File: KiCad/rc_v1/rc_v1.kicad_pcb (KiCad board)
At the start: 2 copper layers, 122 x 46 mm, 36 parts, among them SW1 SLW-1276864-4A-D, SW10 TS12-66, SW11 TS12-1212, SW12 TS12-1212, SW3 TS12-66, SW4 TS12-66, SW5 TS12-66, SW6 TS12-66, SW7 TS12-66, SW8 TS12-66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

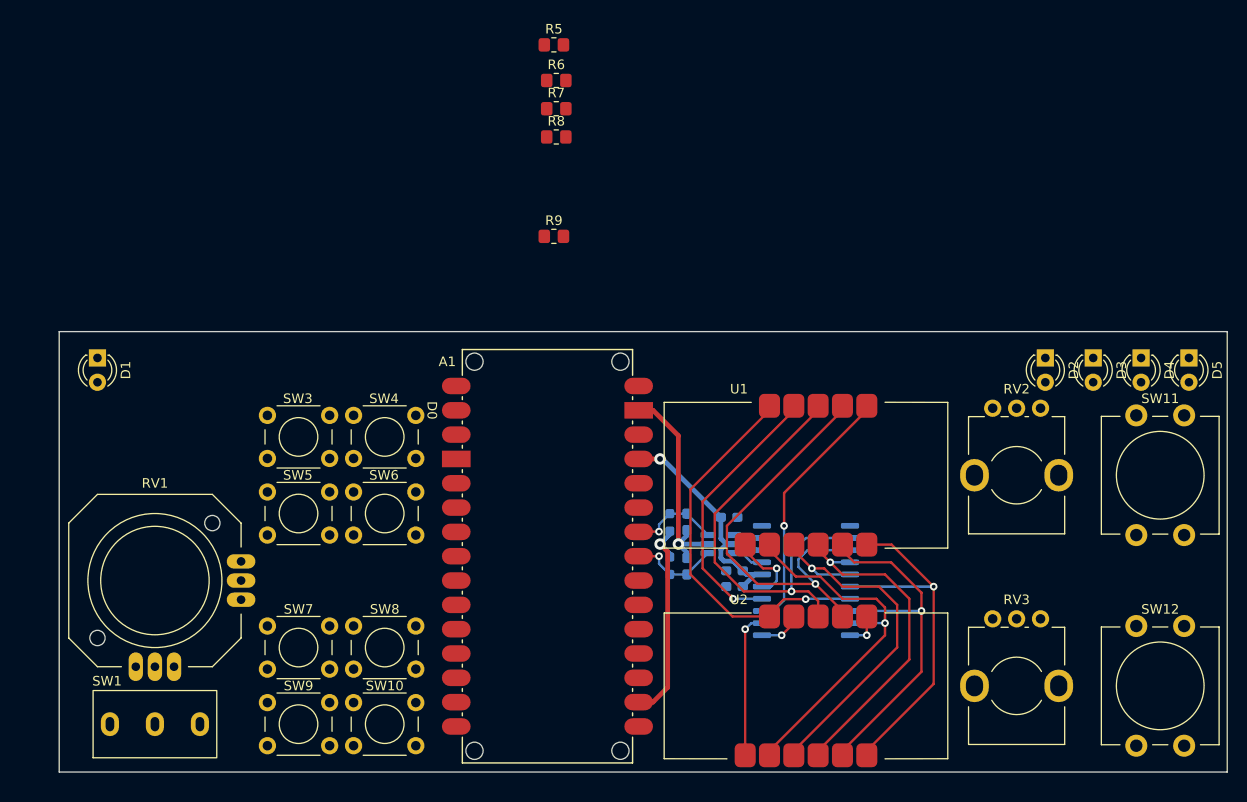
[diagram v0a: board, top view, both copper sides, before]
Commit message: Remote Controller PCB Milestone 2
Routed right side inputs
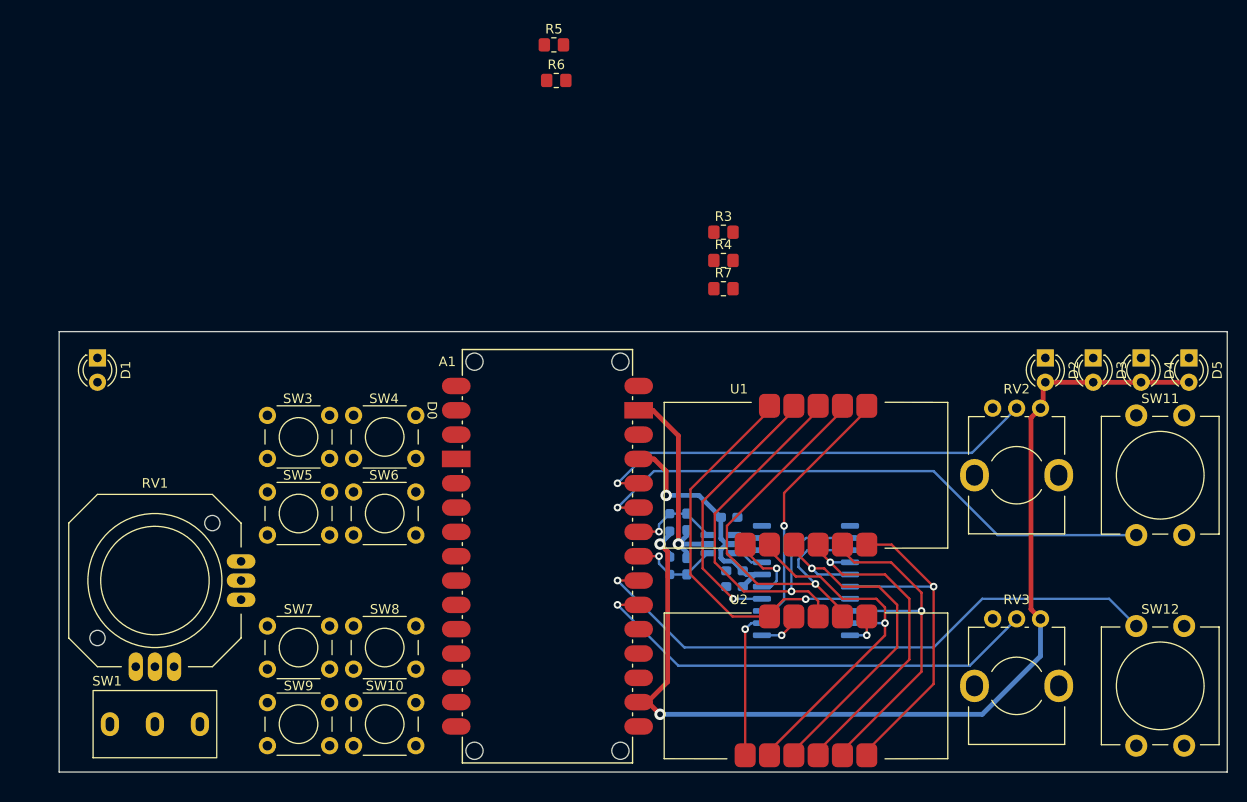
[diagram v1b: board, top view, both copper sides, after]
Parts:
- removed R8, R9: 52.3, Resistor_SMD:R_0805_2012Metric_Pad1.20x1.40mm_HandSolder
- added R3: 52.3, Resistor_SMD:R_0805_2012Metric_Pad1.20x1.40mm_HandSolder, F.Cu at (161.6, 66.5)
- added R4: 52.3, Resistor_SMD:R_0805_2012Metric_Pad1.20x1.40mm_HandSolder, F.Cu at (161.6, 69.4)
- moved R7 25.7 mm to (161.6, 72.4)
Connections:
- A1 pad A0: unconnected-(A1-PadA0) -> /A0
- A1 pad A1: unconnected-(A1-PadA1) -> /A1
- A1 pad A2: unconnected-(A1-PadA2) -> /A2
- A1 pad A3: unconnected-(A1-PadA3) -> /A3
- A1 pad A6: unconnected-(A1-PadA6) -> /A6
- A1 pad A7: unconnected-(A1-PadA7) -> /A7
- D2 pad 1: unconnected-(D2-K-Pad1) -> Net-(D2-K)
- D2 pad 2: unconnected-(D2-A-Pad2) -> +3.3V
- D3 pad 1: unconnected-(D3-K-Pad1) -> Net-(D3-K)
- D3 pad 2: unconnected-(D3-A-Pad2) -> +3.3V
- D4 pad 1: unconnected-(D4-K-Pad1) -> Net-(D4-K)
- D4 pad 2: unconnected-(D4-A-Pad2) -> +3.3V
- D5 pad 1: unconnected-(D5-K-Pad1) -> Net-(D5-K)
- D5 pad 2: unconnected-(D5-A-Pad2) -> +3.3V
- R5 pad 1: unconnected-(R5-Pad1) -> Net-(D3-K)
- R6 pad 1: unconnected-(R6-Pad1) -> Net-(D4-K)
- R7 pad 1: unconnected-(R7-Pad1) -> Net-(D5-K)
- RV2 pad 1: unconnected-(RV2-Pad1) -> +3.3V
- RV2 pad 2: unconnected-(RV2-Pad2) -> /A7
- RV2 pad 3: unconnected-(RV2-Pad3) -> GND
- RV3 pad 1: unconnected-(RV3-Pad1) -> +3.3V
- RV3 pad 2: unconnected-(RV3-Pad2) -> /A2
- RV3 pad 3: unconnected-(RV3-Pad3) -> GND
- SW11 pad 1: unconnected-(SW11-Pad1) -> /A6
- SW11 pad 2: unconnected-(SW11-Pad2) -> GND
- SW12 pad 1: unconnected-(SW12-Pad1) -> /A3
- SW12 pad 2: unconnected-(SW12-Pad2) -> GND
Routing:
- net +3.3V: track 22.5 -> 111.8 mm, vias 1 -> 2
- net /A3: track 0.00 -> 62.6 mm, vias 0 -> 1
- net /A6: track 0.00 -> 60.7 mm, vias 0 -> 1
- net /A2: track 0.00 -> 48.6 mm, vias 0 -> 1
- net /A7: track 0.00 -> 47.1 mm, vias 0 -> 1
- net +5V: track 24.1 -> 25.6 mm

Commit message: Remote Controller PCB Milestone 3
Tentatively completed all connections
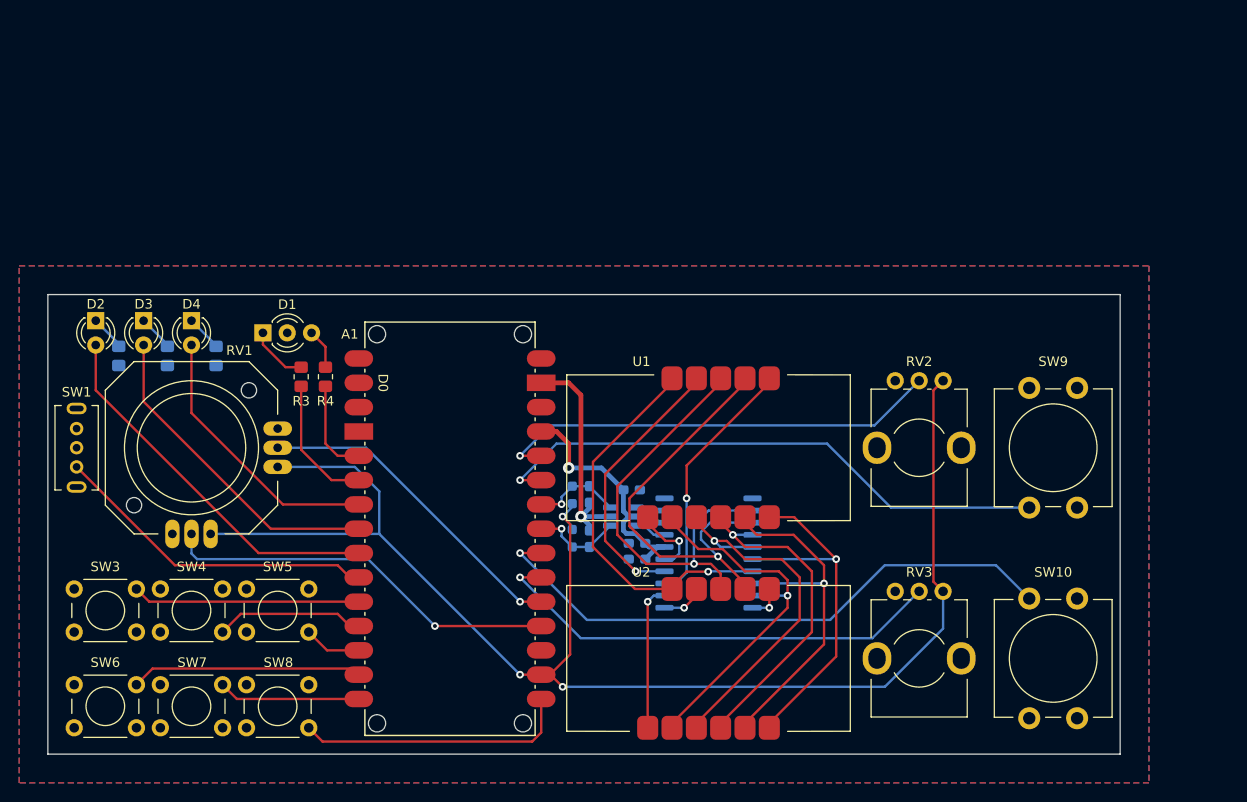
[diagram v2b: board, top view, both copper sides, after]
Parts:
- removed D5: 151031, LED_THT:LED_D3.0mm
- removed the SW10 at (122.9, 115.6)
- removed the SW9 at (113.9, 115.6)
- D1: value 151031 -> LTL1BEKVJNN; footprint LED_THT:LED_D3.0mm -> LED_THT:LED_D3.0mm-3
- R5, R6, R7: moved to B.Cu
- SW1: value SLW-1276864-4A-D -> OS102011MS2Qxxx; footprint Footprint Library:SW_Slide_SPDT_CIT_SLW-1276864-4A-D -> Footprint Library:SW_Slide_SPDT_CK_OS102011MS2Qxxx
- moved D2 99.3 mm to (96.0, 75.7)
- moved D3 99.3 mm to (101.0, 75.7)
- moved D4 99.3 mm to (106.0, 75.7)
- moved R5 55.9 mm to (98.4, 79.4), turned to -90 degrees
- moved R7 53.5 mm to (108.6, 79.4), turned to -90 degrees
- moved R6 49.8 mm to (103.5, 79.4), turned to -90 degrees
- moved R3 46.6 mm to (117.5, 81.6), turned to 90 degrees
- moved R4 43.3 mm to (120.0, 81.6), turned to 90 degrees
- moved SW6 35.4 mm to (93.8, 113.8)
- moved SW1 31.1 mm to (94.0, 87.0), turned to 0 degrees
- moved SW3 27.1 mm to (93.8, 103.8)
- moved SW4 27.1 mm to (102.8, 103.8)
- moved D1 17.5 mm to (113.5, 77.0), turned to 0 degrees
- moved RV1 14.4 mm to (106.0, 89.0)
- moved SW7 12.8 mm to (102.8, 113.8)
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- renumbered SW12 to SW10, SW11 to SW9
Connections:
- A1 pad D10: unconnected-(A1-PadD10) -> /D10
- A1 pad D11: unconnected-(A1-D11_MOSI-PadD11) -> /D11
- A1 pad D12: unconnected-(A1-D12_MISO-PadD12) -> /D12
- A1 pad D13: unconnected-(A1-D13_SCK-PadD13) -> /D13
- A1 pad D2: unconnected-(A1-PadD2) -> /D2
- A1 pad D3: unconnected-(A1-PadD3) -> /D3
- A1 pad D4: unconnected-(A1-PadD4) -> /D4
- A1 pad D5: unconnected-(A1-PadD5) -> /D5
- A1 pad D6: unconnected-(A1-PadD6) -> /D6
- A1 pad D7: unconnected-(A1-PadD7) -> /D7
- A1 pad D8: unconnected-(A1-PadD8) -> /D8
- A1 pad D9: unconnected-(A1-PadD9) -> /D9
- D1 pad 1: unconnected-(D1-K-Pad1) -> Net-(D1-A1)
- D1 pad 2: unconnected-(D1-A-Pad2) -> GND
- D2 pad 2: +3.3V -> /D6
- D3 pad 2: +3.3V -> /D5
- D4 pad 2: +3.3V -> /D4
- R3 pad 1: unconnected-(R3-Pad1) -> /D3
- R3 pad 2: unconnected-(R3-Pad2) -> Net-(D1-A1)
- R4 pad 1: Net-(D2-K) -> /D2
- R4 pad 2: unconnected-(R4-Pad2) -> Net-(D1-A2)
- R5 pad 1: Net-(D3-K) -> Net-(D2-K)
- R5 pad 2: unconnected-(R5-Pad2) -> GND
- R6 pad 1: Net-(D4-K) -> Net-(D3-K)
- R6 pad 2: unconnected-(R6-Pad2) -> GND
- R7 pad 1: Net-(D5-K) -> Net-(D4-K)
- R7 pad 2: unconnected-(R7-Pad2) -> GND
- RV1 pad 1: unconnected-(RV1-Pad1) -> GND
- RV1 pad 2: unconnected-(RV1-Pad2) -> /A1
- RV1 pad 3: unconnected-(RV1-Pad3) -> +3.3V
- RV1 pad 4: unconnected-(RV1-Pad4) -> GND
- RV1 pad 5: unconnected-(RV1-Pad5) -> /A0
- RV1 pad 6: unconnected-(RV1-Pad6) -> +3.3V
- SW1 pad 2: unconnected-(SW1-B-Pad2) -> GND
- SW1 pad 3: unconnected-(SW1-C-Pad3) -> /D7
- SW3 pad 1: unconnected-(SW3-Pad1) -> /D8
- SW3 pad 2: unconnected-(SW3-Pad2) -> GND
- SW4 pad 1: unconnected-(SW4-Pad1) -> GND
- SW4 pad 2: unconnected-(SW4-Pad2) -> /D9
- SW5 pad 1: unconnected-(SW5-Pad1) -> GND
- SW5 pad 2: unconnected-(SW5-Pad2) -> /D10
- SW6 pad 1: unconnected-(SW6-Pad1) -> /D11
- SW6 pad 2: unconnected-(SW6-Pad2) -> GND
- SW7 pad 1: unconnected-(SW7-Pad1) -> /D12
- SW7 pad 2: unconnected-(SW7-Pad2) -> GND
- SW8 pad 1: unconnected-(SW8-Pad1) -> GND
- SW8 pad 2: unconnected-(SW8-Pad2) -> /D13
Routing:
- net /A0: track 0.00 -> 41.7 mm, vias 0 -> 1
- net /D6: track 0.00 -> 39.2 mm
- net +3.3V: track 111.8 -> 150.6 mm, vias 2 -> 3
- net /D7: track 0.00 -> 34.3 mm
- net /A1: track 0.00 -> 34.2 mm, vias 0 -> 1
- net /D5: track 0.00 -> 33.9 mm
- net /D13: track 0.00 -> 28.8 mm
- net /D4: track 0.00 -> 28.5 mm
- net /D11: track 0.00 -> 24.2 mm
- net /D8: track 0.00 -> 23.8 mm
- net /D9: track 0.00 -> 15.5 mm
- net /D12: track 0.00 -> 14.8 mm
- net /D3: track 0.00 -> 14.0 mm
- net /D2: track 0.00 -> 9.99 mm
- net Net-(D1-A1): track 0.00 -> 6.20 mm
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- added copper zone on B.Cu, net GND
- added copper zone on F.Cu, net GND
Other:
- board size 122 x 46 mm -> 112 x 48 mm

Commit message: Backup
Will replace buffer with level shifter
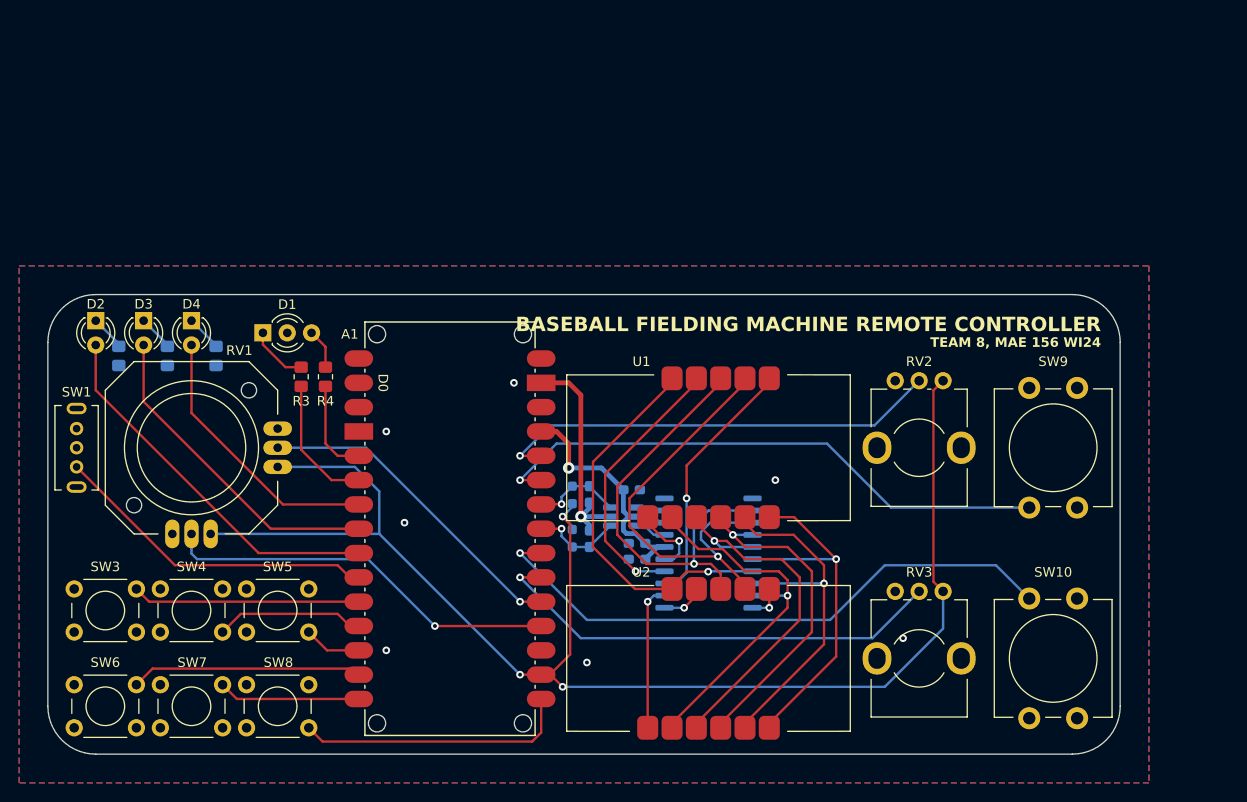
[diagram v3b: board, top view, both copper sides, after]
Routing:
- net GND: vias 1 -> 8
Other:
- outline, holes or cut-outs redrawn
- board text added: "BASEBALL FIELDING MACHINE REMOTE CONTROLLER"
- board text added: "D.H.L. REV. 0 01/04/2024"
- board text added: "TEAM 8, MAE 156 WI24"

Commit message: Remote Controller PCB Milestone 5
Added level shifter IC, prototype board nearly completed
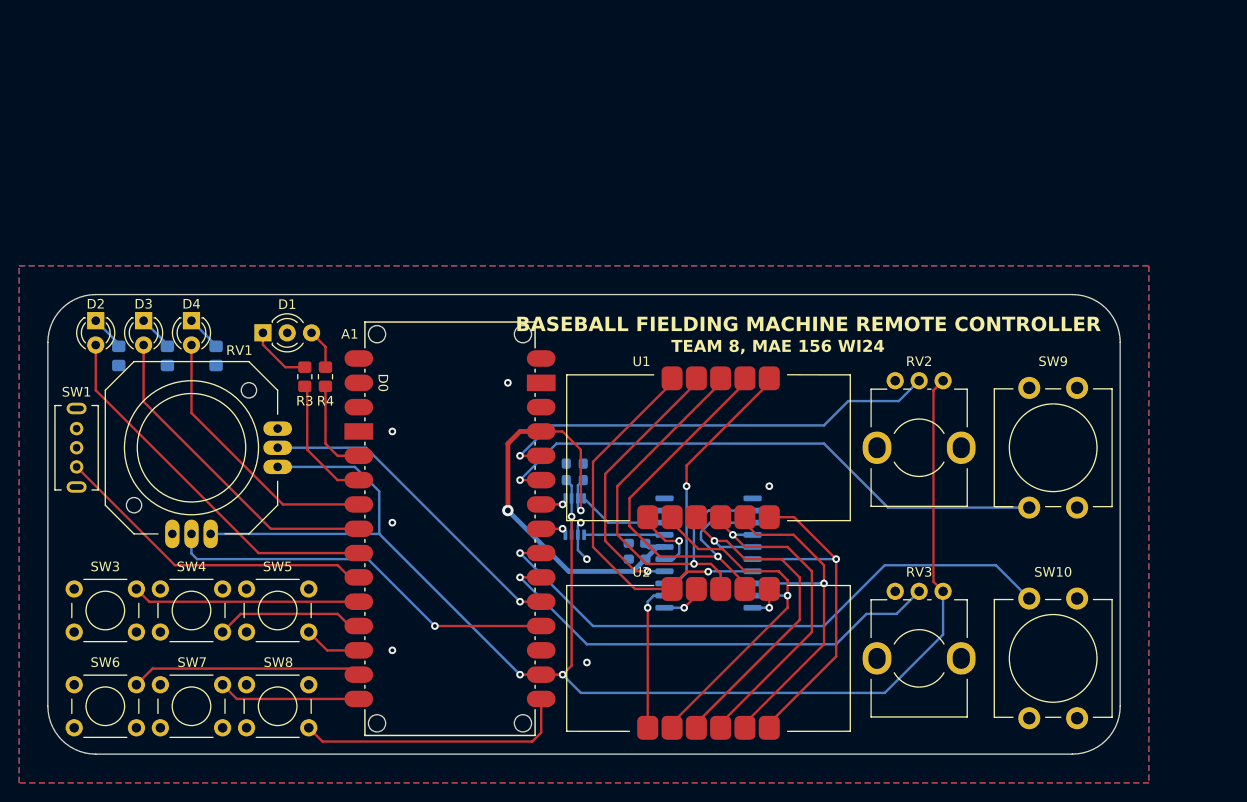
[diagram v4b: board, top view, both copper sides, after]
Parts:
- removed C5: 0.1u, Capacitor_SMD:C_0603_1608Metric_Pad1.08x0.95mm_HandSolder
- removed R1, R2: 10k, Resistor_SMD:R_0603_1608Metric_Pad0.98x0.95mm_HandSolder
- removed U6: SN74LVC2G17DBVR, Footprint Library:SOT-23-6_HandSoldering_Rounded
- added U4: TXS0102DCTR, Footprint Library:SSOP-8_2.95x2.8mm_P0.65mm, B.Cu at (146.0, 96.2)
- C3, C4: value 100p -> 0.1u
- moved C4 7.01 mm to (146.9, 91.5)
- moved C3 3.38 mm to (145.1, 91.5), turned to 90 degrees
- moved R3 0.38 mm to (117.8, 81.6)
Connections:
- C3 pad 1: /CLK -> +3.3V
- C4 pad 1: /DIO -> +5V
- U3 pad 17: /DIO_BUF -> /DIO_5V
- U3 pad 18: /CLK_BUF -> /CLK_5V
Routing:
- net +5V: track 25.6 -> 48.0 mm, vias 1 -> 2
- net GND: track 24.1 -> 4.33 mm
- net /CLK_5V: track 0.00 -> 9.45 mm
- net /DIO_5V: track 0.00 -> 8.40 mm
- net /DIO: track 9.43 -> 2.99 mm
- net /CLK: track 9.40 -> 2.99 mm
- net /CLK_BUF: track 3.60 -> 0.00 mm
- net /DIO_BUF: track 3.34 -> 0.00 mm
- net +3.3V: track 150.6 -> 152.2 mm
- net /D3: track 14.0 -> 13.4 mm
- net /A3: track 62.1 -> 62.6 mm
- net /A2: track 48.6 -> 49.1 mm
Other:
- board text added: "D.H.L. REV. 0 01/06/2024"
- board text removed: "D.H.L. REV. 0 01/04/2024"

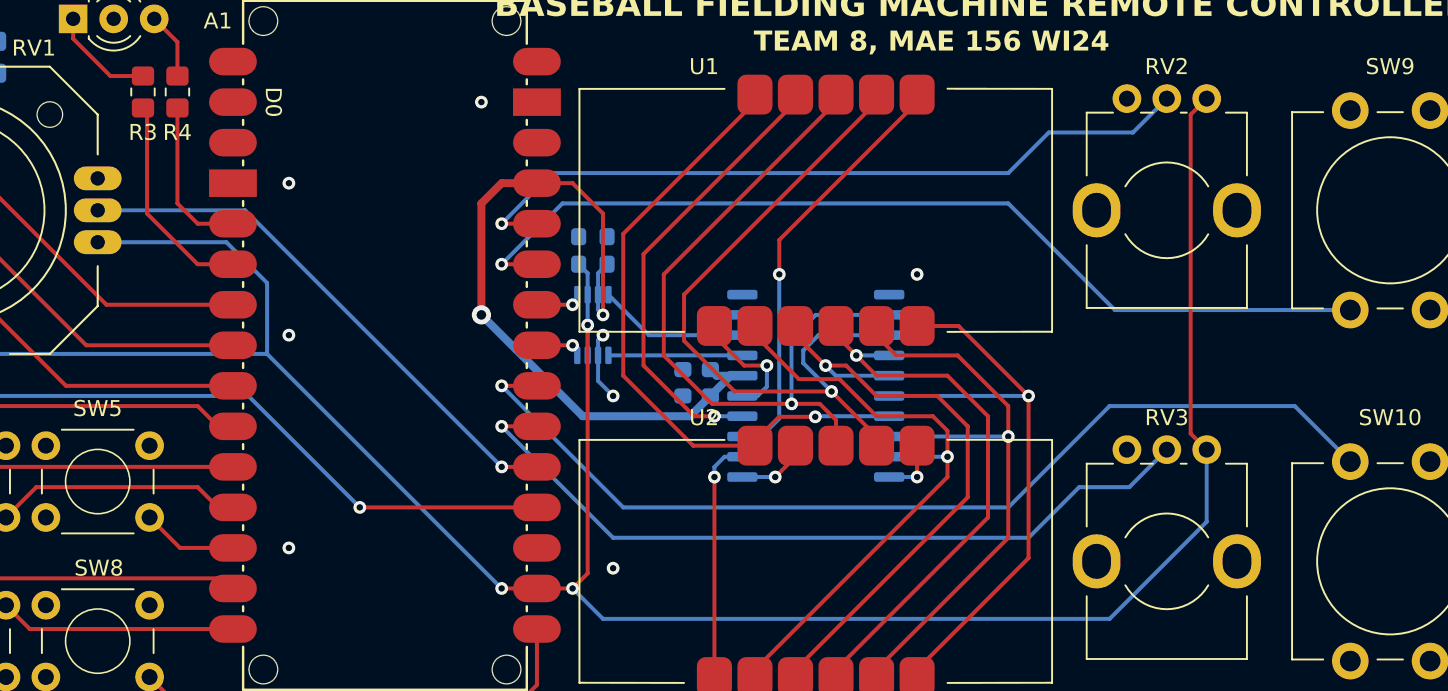
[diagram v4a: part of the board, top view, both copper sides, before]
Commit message: Remote Controller PCB Milestone 6
Added GPIO output to OE input pin
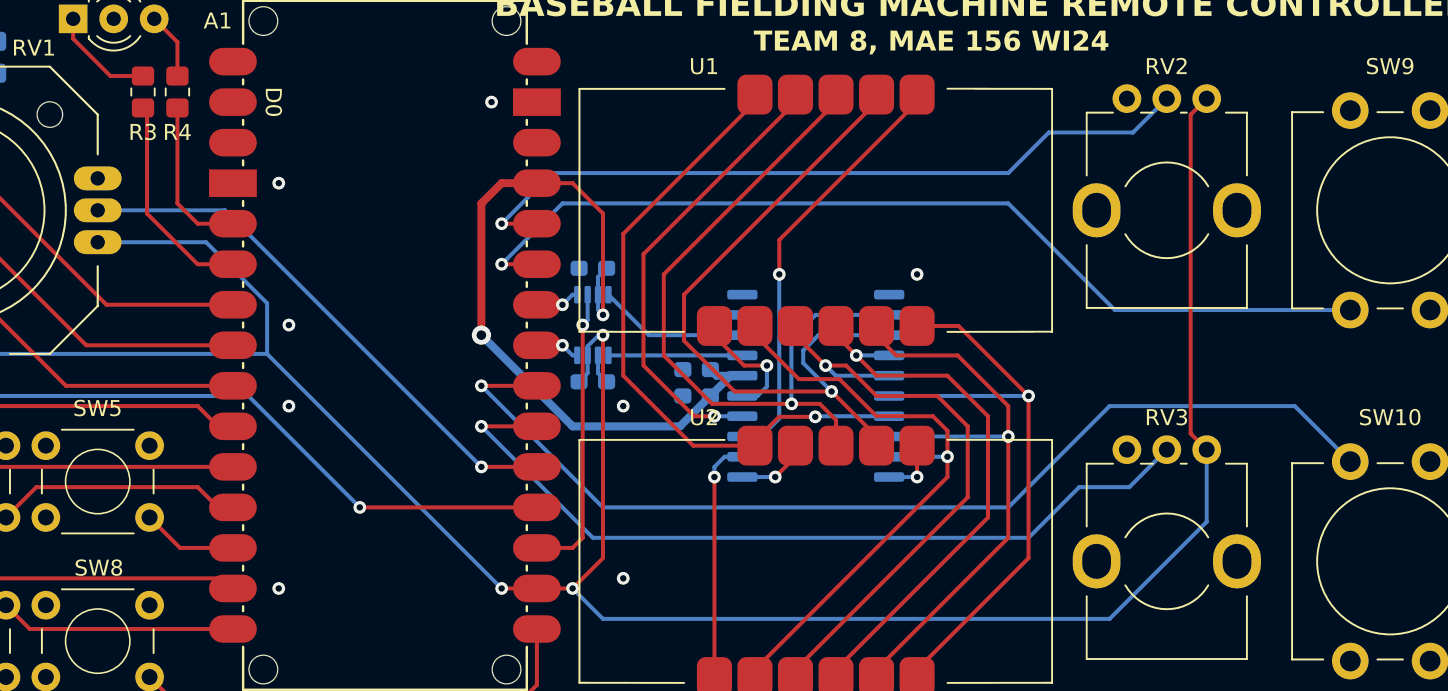
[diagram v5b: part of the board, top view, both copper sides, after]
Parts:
- moved C3 8.28 mm to (146.0, 99.7), turned to 0 degrees
- moved C4 1.43 mm to (146.0, 92.6), turned to 180 degrees
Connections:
- A1 pad B0: unconnected-(A1-PadB0) -> /OE
- U4 pad 6: +3.3V -> /OE
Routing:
- net /OE: track 0.00 -> 18.5 mm, vias 0 -> 1
- net +3.3V: track 152.2 -> 149.0 mm
- net /A2: track 49.1 -> 51.6 mm
- net /A3: track 62.6 -> 65.2 mm
- net GND: track 4.33 -> 1.88 mm
- net +5V: track 48.0 -> 49.0 mm

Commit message: Design v1 Finished
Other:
- board text added: "D.H.L. REV. 0 01/07/2024"
- board text removed: "D.H.L. REV. 0 01/06/2024"
